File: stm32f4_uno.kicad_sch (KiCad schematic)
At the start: 48 parts, among them J1 Barrel_Jack, J101 Digital/PWM, J102 Power, J103 Analog, J104 Digital/PWM, J106 Ethernet, J107 Digital/PWM, J108 Analog, J109 Power, J110 Digital/PWM, J111 Digital/PWM, J4 Conn_ST_STDC14, U101 STM32F407VGTx, Y3 32.768kHz, Y4 25MHz

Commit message: WIP
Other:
- moved on the sheet: J106, J107
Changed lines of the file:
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@@
     (stroke (width 0) (type default))
   )
-  (wire (pts (xy 169.545 27.305) (xy 180.34 27.305))
+  (wire (pts (xy 169.545 50.165) (xy 180.34 50.165))
     (stroke (width 0) (type default))
   )
@@
     (effects (font (size 1 1)) (justify right bottom))
   )
-  (label "PB2" (at 169.545 73.025 0) (fields_autoplaced)
+  (label "PB2" (at 169.545 39.37 0) (fields_autoplaced)
     (effects (font (size 1 1)) (justify left bottom))
   )
@@
     (effects (font (size 1 1)) (justify left bottom))
   )
-  (label "ETH_MDIO" (at 169.545 45.085 0) (fields_autoplaced)
+  (label "ETH_MDIO" (at 169.545 67.945 0) (fields_autoplaced)
     (effects (font (size 1 1)) (justify left bottom))
   )
@@
     (effects (font (size 1 1)) (justify left bottom))
   )
-  (label "ETH_TXD1" (at 169.545 29.845 0) (fields_autoplaced)
+  (label "ETH_TXD1" (at 169.545 52.705 0) (fields_autoplaced)
     (effects (font (size 1 1)) (justify left bottom))
   )
@@
     (effects (font (size 1 1)) (justify right bottom))
   )
-  (label "ETH_MDC" (at 169.545 50.165 0) (fields_autoplaced)
-    (effects (font (size 1 1)) (justify left bottom))
-  )
-  (label "PA3" (at 169.545 78.105 0) (fields_autoplaced)
+  (label "ETH_MDC" (at 169.545 73.025 0) (fields_autoplaced)
+    (effects (font (size 1 1)) (justify left bottom))
+  )
+  (label "PA3" (at 169.545 44.45 0) (fields_autoplaced)
     (effects (font (size 1 1)) (justify left bottom))
   )
@@
     (effects (font (size 1 1)) (justify right bottom))
   )
-  (label "PB14" (at 169.545 60.325 0) (fields_autoplaced)
+  (label "PB14" (at 169.545 26.67 0) (fields_autoplaced)
     (effects (font (size 1 1)) (justify left bottom))
   )
@@
     (effects (font (size 1 1)) (justify right bottom))
   )
-  (label "ETH_RXD0" (at 169.545 40.005 0) (fields_autoplaced)
+  (label "ETH_RXD0" (at 169.545 62.865 0) (fields_autoplaced)
     (effects (font (size 1 1)) (justify left bottom))
   )
@@
     (effects (font (size 1 1)) (justify right bottom))
   )
-  (label "PE12" (at 169.545 65.405 0) (fields_autoplaced)
+  (label "PE12" (at 169.545 31.75 0) (fields_autoplaced)
     (effects (font (size 1 1)) (justify left bottom))
   )
@@
     (effects (font (size 1 1)) (justify right bottom))
   )
-  (label "PE14" (at 169.545 62.865 0) (fields_autoplaced)
+  (label "PE14" (at 169.545 29.21 0) (fields_autoplaced)
     (effects (font (size 1 1)) (justify left bottom))
   )
@@
     (effects (font (size 1 1)) (justify left bottom))
   )
-  (label "PE7" (at 169.545 70.485 0) (fields_autoplaced)
+  (label "PE7" (at 169.545 36.83 0) (fields_autoplaced)
     (effects (font (size 1 1)) (justify left bottom))
   )
@@
     (effects (font (size 1 1)) (justify left bottom))
   )
-  (label "ETH_CRS_DV" (at 169.545 42.545 0) (fields_autoplaced)
+  (label "ETH_CRS_DV" (at 169.545 65.405 0) (fields_autoplaced)
     (effects (font (size 1 1)) (justify left bottom))
   )
@@
     (effects (font (size 1 1)) (justify right bottom))
   )
-  (label "ETH_REF_CLK" (at 169.545 47.625 0) (fields_autoplaced)
+  (label "ETH_REF_CLK" (at 169.545 70.485 0) (fields_autoplaced)
     (effects (font (size 1 1)) (justify left bottom))
   )
@@
     (effects (font (size 1 1)) (justify right bottom))
   )
-  (label "ETH_TX_EN" (at 169.545 34.925 0) (fields_autoplaced)
+  (label "ETH_TX_EN" (at 169.545 57.785 0) (fields_autoplaced)
     (effects (font (size 1 1)) (justify left bottom))
   )
@@
     (effects (font (size 1 1)) (justify right bottom))
   )
-  (label "ETH_RXD1" (at 169.545 37.465 0) (fields_autoplaced)
+  (label "ETH_RXD1" (at 169.545 60.325 0) (fields_autoplaced)
     (effects (font (size 1 1)) (justify left bottom))
   )
@@
     (effects (font (size 1 1)) (justify right bottom))
   )
-  (label "ETH_TXD0" (at 169.545 32.385 0) (fields_autoplaced)
+  (label "ETH_TXD0" (at 169.545 55.245 0) (fields_autoplaced)
     (effects (font (size 1 1)) (justify left bottom))
   )
@@
     (effects (font (size 1 1)) (justify left bottom))
   )
-  (label "PB0" (at 169.545 75.565 0) (fields_autoplaced)
+  (label "PB0" (at 169.545 41.91 0) (fields_autoplaced)
     (effects (font (size 1 1)) (justify left bottom))
   )
@@
     (effects (font (size 1 1)) (justify left bottom))
   )
-  (label "PE10" (at 169.545 67.945 0) (fields_autoplaced)
+  (label "PE10" (at 169.545 34.29 0) (fields_autoplaced)
     (effects (font (size 1 1)) (justify left bottom))
   )
@@
     )
   )
-  (symbol (lib_id "Connector_Generic:Conn_01x10") (at 164.465 37.465 0) (mirror y) (unit 1)
-    (in_bom yes) (on_board yes) (dnp no)
-    (property "Reference" "J106" (at 164.465 24.765 0)
-      (effects (font (size 1 1)))
-    )
-    (property "Value" "Ethernet" (at 161.925 37.465 90)
-      (effects (font (size 1 1)))
-    )
-    (property "Footprint" "Connector_PinSocket_2.54mm:PinSocket_1x10_P2.54mm_Vertical" (at 164.465 37.465 0)
-      (effects (font (size 1 1)) hide)
-    )
-    (property "Datasheet" "" (at 164.465 37.465 0)
-      (effects (font (size 1 1)))
-    )
-    (property "Description" "" (at 164.465 37.465 0)
-      (effects (font (size 1.27 1.27)) hide)
-    )
-    (property "Manufacturer" "" (at 164.465 37.465 0)
-      (effects (font (size 1.27 1.27)) hide)
-    )
-    (property "Partnumber" "" (at 164.465 37.465 0)
-      (effects (font (size 1.27 1.27)) hide)
-    )
-    (property "JLCPCB Part #" "" (at 164.465 37.465 0)
-      (effects (font (size 1.27 1.27)) hide)
-    )
-    (property "isBasicPart" "" (at 164.465 37.465 0)
+  (symbol (lib_id "Connector_Generic:Conn_01x10") (at 164.465 60.325 0) (mirror y) (unit 1)
+    (in_bom yes) (on_board yes) (dnp no)
+    (property "Reference" "J106" (at 164.465 47.625 0)
+      (effects (font (size 1 1)))
+    )
+    (property "Value" "Ethernet" (at 161.925 60.325 90)
+      (effects (font (size 1 1)))
+    )
+    (property "Footprint" "Connector_PinSocket_2.54mm:PinSocket_1x10_P2.54mm_Vertical" (at 164.465 60.325 0)
+      (effects (font (size 1 1)) hide)
+    )
+    (property "Datasheet" "" (at 164.465 60.325 0)
+      (effects (font (size 1 1)))
+    )
+    (property "Description" "" (at 164.465 60.325 0)
+      (effects (font (size 1.27 1.27)) hide)
+    )
+    (property "Manufacturer" "" (at 164.465 60.325 0)
+      (effects (font (size 1.27 1.27)) hide)
+    )
+    (property "Partnumber" "" (at 164.465 60.325 0)
+      (effects (font (size 1.27 1.27)) hide)
+    )
+    (property "JLCPCB Part #" "" (at 164.465 60.325 0)
+      (effects (font (size 1.27 1.27)) hide)
+    )
+    (property "isBasicPart" "" (at 164.465 60.325 0)
       (effects (font (size 1.27 1.27)) hide)
     )
@@
     )
   )
-  (symbol (lib_id "Connector_Generic:Conn_01x08") (at 164.465 67.945 0) (mirror y) (unit 1)
-    (in_bom yes) (on_board yes) (dnp no)
-    (property "Reference" "J107" (at 164.465 57.785 0)
-      (effects (font (size 1 1)))
-    )
-    (property "Value" "Digital/PWM" (at 161.925 67.945 90)
-      (effects (font (size 1 1)))
-    )
-    (property "Footprint" "Connector_PinSocket_2.54mm:PinSocket_1x08_P2.54mm_Vertical" (at 164.465 67.945 0)
-      (effects (font (size 1 1)) hide)
-    )
-    (property "Datasheet" "" (at 164.465 67.945 0)
+  (symbol (lib_id "Connector_Generic:Conn_01x08") (at 164.465 34.29 0) (mirror y) (unit 1)
+    (in_bom yes) (on_board yes) (dnp no)
+    (property "Reference" "J107" (at 164.465 24.13 0)
+      (effects (font (size 1 1)))
+    )
+    (property "Value" "Digital/PWM" (at 161.925 34.29 90)
+      (effects (font (size 1 1)))
+    )
+    (property "Footprint" "Connector_PinSocket_2.54mm:PinSocket_1x08_P2.54mm_Vertical" (at 164.465 34.29 0)
+      (effects (font (size 1 1)) hide)
+    )
+    (property "Datasheet" "" (at 164.465 34.29 0)
       (effects (font (size 1 1)))
     )
@@
     )
   )
-  (symbol (lib_id "power:GND") (at 180.34 27.305 90) (unit 1)
-    (in_bom yes) (on_board yes) (dnp no)
-    (property "Reference" "#PWR0126" (at 186.69 27.305 0)
-      (effects (font (size 1 1)) hide)
-    )
-    (property "Value" "GND" (at 184.785 27.305 90)
-      (effects (font (size 1 1)))
-    )
-    (property "Footprint" "" (at 180.34 27.305 0)
-      (effects (font (size 1 1)))
-    )
-    (property "Datasheet" "" (at 180.34 27.305 0)
-      (effects (font (size 1 1)))
-    )
+  (symbol (lib_id "power:GND") (at 180.34 50.165 90) (unit 1)
+    (in_bom yes) (on_board yes) (dnp no)
+    (property "Reference" "#PWR0126" (at 186.69 50.165 0)
+      (effects (font (size 1 1)) hide)
+    )
+    (property "Value" "GND" (at 184.785 50.165 90)
+      (effects (font (size 1 1)))
+    )
+    (property "Footprint" "" (at 180.34 50.165 0)
+      (effects (font (size 1 1)))
+    )
+    (property "Datasheet" "" (at 180.34 50.165 0)
+      (effects (font (size 1 1)))
+    )

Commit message: First version done
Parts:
- J1: symbol Connector:Barrel_Jack -> Connector:Barrel_Jack_Switch; Manufacturer (none) -> CUI Devices; Partnumber (none) -> PJ-102AH; isBasicPart (none) -> NO; now in the parts list
- J107, J110, J111: value Digital/PWM -> STM32 GPIO
- J108: value Analog -> STM32 GPIO
- J109: value Power -> STM32 GPIO
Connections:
- no-connect marks 4 -> 5
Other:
- moved on the sheet: J101, J102, J103, J104, J106, J107, J108, J109, J110, J111

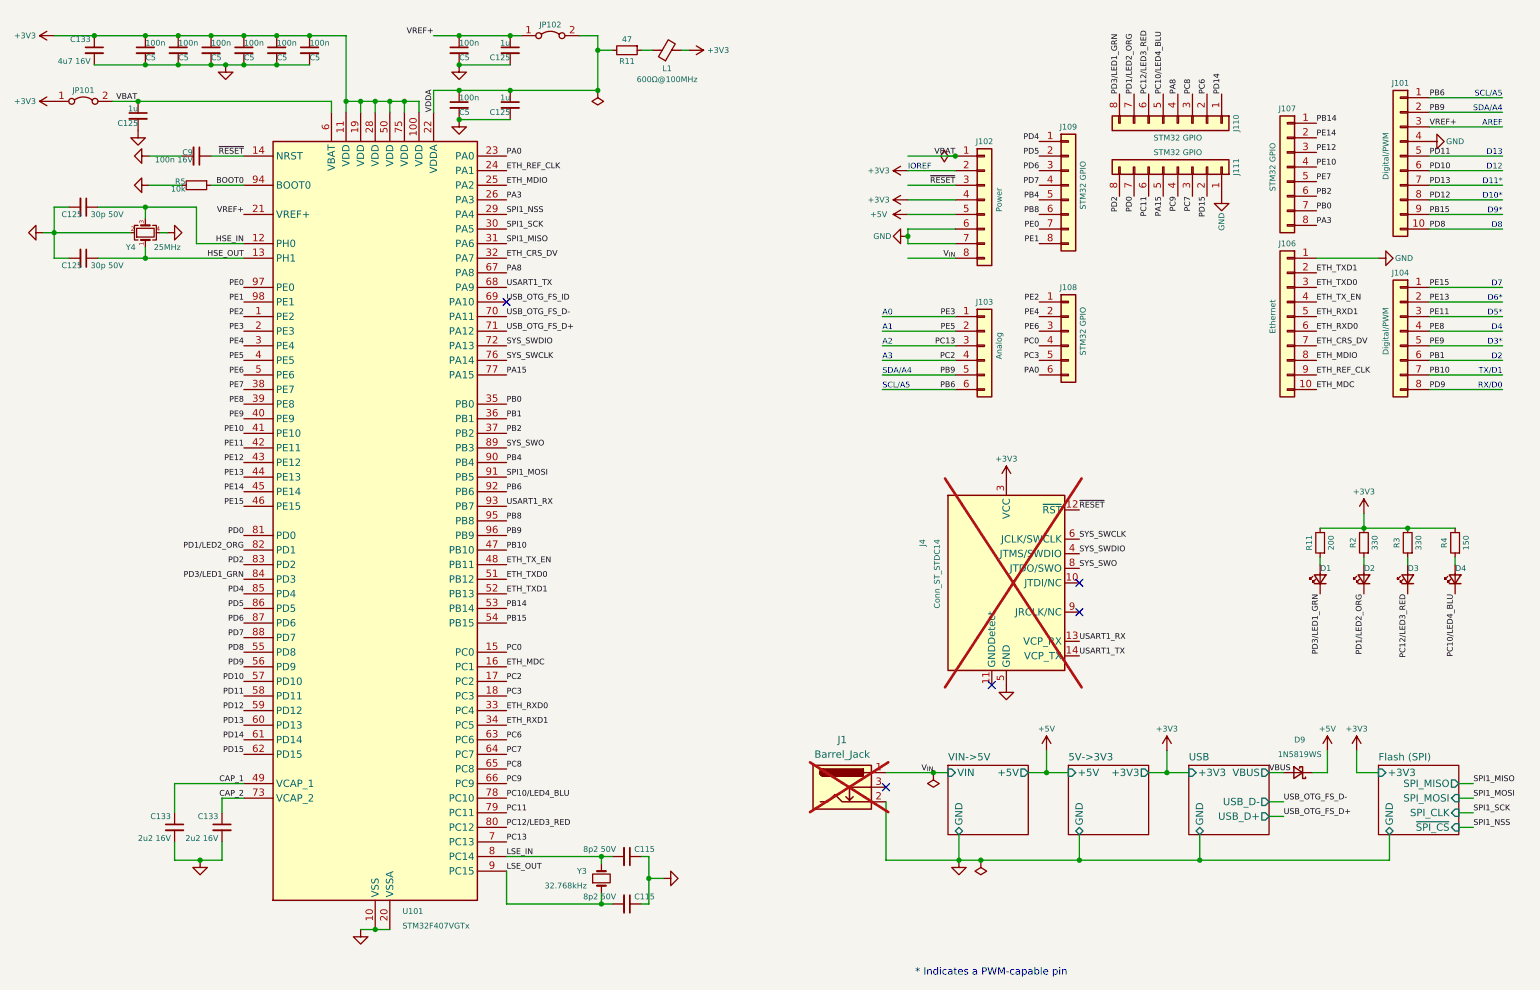
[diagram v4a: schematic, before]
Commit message: Add ETH_RXER
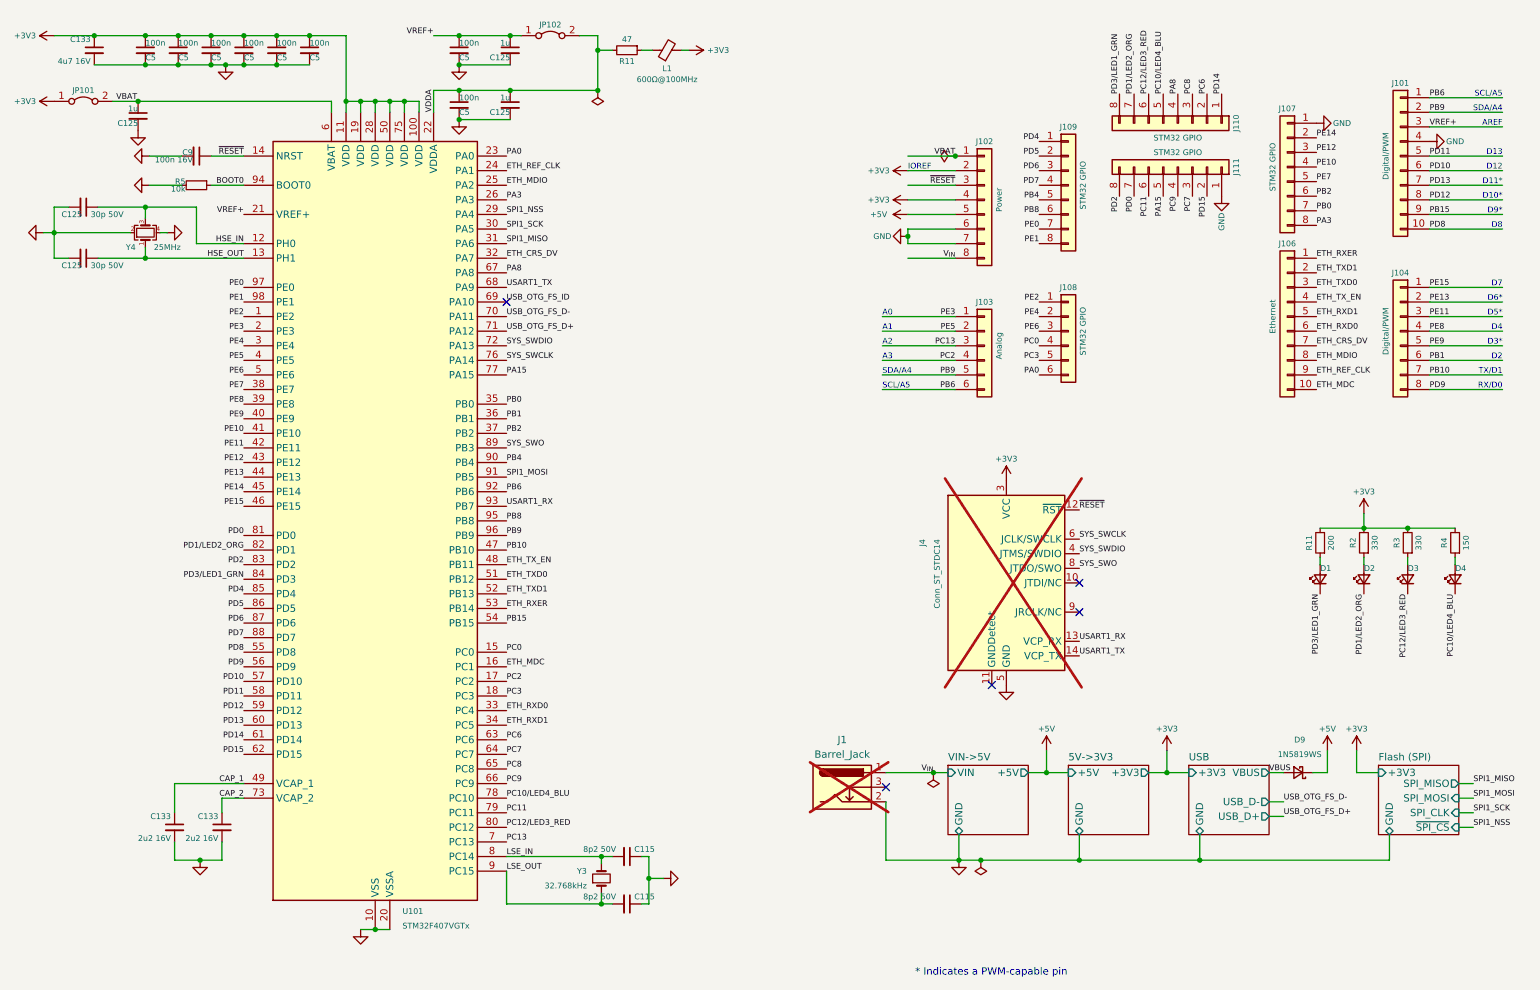
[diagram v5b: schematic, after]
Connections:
- net GND: now also J107.1 (Pin_1); no longer J106.1 (Pin_1)
- net PB14 renamed ETH_RXER
- net ETH_RXER: now also J106.1 (Pin_1); no longer J107.1 (Pin_1)
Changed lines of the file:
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@@
     (stroke (width 0) (type default))
   )
-  (wire (pts (xy 247.65 55.245) (xy 258.445 55.245))
-    (stroke (width 0) (type default))
-  )
   (wire (pts (xy 57.785 21.59) (xy 60.96 21.59))
     (stroke (width 0) (type default))
@@
     (effects (font (size 1 1)) (justify right bottom))
   )
+  (label "PA3" (at 247.65 49.53 0) (fields_autoplaced)
+    (effects (font (size 1 1)) (justify left bottom))
+  )
   (label "ETH_TXD0" (at 106.68 111.125 0) (fields_autoplaced)
     (effects (font (size 1 1)) (justify left bottom))
@@
     (effects (font (size 1 1)) (justify right bottom))
   )
+  (label "ETH_RXER" (at 247.65 55.245 0) (fields_autoplaced)
+    (effects (font (size 1 1)) (justify left bottom))
+  )
+  (label "ETH_RXER" (at 106.68 116.205 0) (fields_autoplaced)
+    (effects (font (size 1 1)) (justify left bottom))
+  )
   (label "PB15" (at 106.68 118.745 0) (fields_autoplaced)
     (effects (font (size 1 1)) (justify left bottom))
@@
     (effects (font (size 1 1)) (justify left bottom))
   )
-  (label "PA3" (at 247.65 49.53 0) (fields_autoplaced)
-    (effects (font (size 1 1)) (justify left bottom))
-  )
   (label "PD4" (at 60.96 113.665 180) (fields_autoplaced)
     (effects (font (size 1 1)) (justify right bottom))
@@
     (effects (font (size 1 1)) (justify right bottom))
   )
-  (label "PB14" (at 247.65 31.75 0) (fields_autoplaced)
-    (effects (font (size 1 1)) (justify left bottom))
-  )
   (label "PE10" (at 60.96 85.725 180) (fields_autoplaced)
     (effects (font (size 1 1)) (justify right bottom))
@@
     (effects (font (size 1 1)) (justify right bottom))
   )
+  (label "PA3" (at 106.68 45.085 0) (fields_autoplaced)
+    (effects (font (size 1 1)) (justify left bottom))
+  )
   (label "PB6" (at 106.68 95.885 0) (fields_autoplaced)
     (effects (font (size 1 1)) (justify left bottom))
@@
     (effects (font (size 1 1)) (justify left bottom))
   )
-  (label "PA3" (at 106.68 45.085 0) (fields_autoplaced)
-    (effects (font (size 1 1)) (justify left bottom))
-  )
   (label "PE1" (at 60.96 62.865 180) (fields_autoplaced)
     (effects (font (size 1 1)) (justify right bottom))
@@
     (effects (font (size 1 1)) (justify left bottom))
   )
-  (label "PB14" (at 106.68 116.205 0) (fields_autoplaced)
-    (effects (font (size 1 1)) (justify left bottom))
-  )
   (label "SYS_SWDIO" (at 106.68 70.485 0) (fields_autoplaced)
     (effects (font (size 1 1)) (justify left bottom))
@@
     )
   )
-  (symbol (lib_id "power:GND") (at 258.445 55.245 90) (unit 1)
-    (in_bom yes) (on_board yes) (dnp no)
-    (property "Reference" "#PWR0126" (at 264.795 55.245 0)
-      (effects (font (size 1 1)) hide)
-    )
-    (property "Value" "GND" (at 262.89 55.245 90)
-      (effects (font (size 1 1)))
-    )
-    (property "Footprint" "" (at 258.445 55.245 0)
-      (effects (font (size 1 1)))
-    )
-    (property "Datasheet" "" (at 258.445 55.245 0)
-      (effects (font (size 1 1)))
-    )
-    (pin "1")
-    (instances
-      (project "stm32f4_uno"
-        (path "/e63e39d7-6ac0-4ffd-8aa3-1841a4541b55"
-          (reference "#PWR0126") (unit 1)
-        )
-      )
-    )
-  )
   (symbol (lib_id "power:GND") (at 98.425 31.115 0) (unit 1)
     (in_bom yes) (on_board yes) (dnp no) (fields_autoplaced)
@@
         )
       )
+    )
+  )
+  (symbol (lib_id "power:GND") (at 247.65 31.75 90) (unit 1)
+    (in_bom yes) (on_board yes) (dnp no)
+    (property "Reference" "#PWR0126" (at 254 31.75 0)
+      (effects (font (size 1 1)) hide)
+    )
+    (property "Value" "GND" (at 252.095 31.75 90)
+      (effects (font (size 1 1)))
+    )
+    (property "Footprint" "" (at 247.65 31.75 0)
+      (effects (font (size 1 1)))
+    )
+    (property "Datasheet" "" (at 247.65 31.75 0)
+      (effects (font (size 1 1)))
+    )
+    (pin "1")
+    (instances
+      (project "stm32f4_uno"
+        (path "/e63e39d7-6ac0-4ffd-8aa3-1841a4541b55"
+          (reference "#PWR0126") (unit 1)
+        )
+      )
